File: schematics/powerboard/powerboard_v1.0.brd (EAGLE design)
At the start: 50 x 50 mm, 38 parts, among them IC1 ACS756LCB-100B-PFF-T, IC2 ATMEGA644-A, Y1 10MHZ

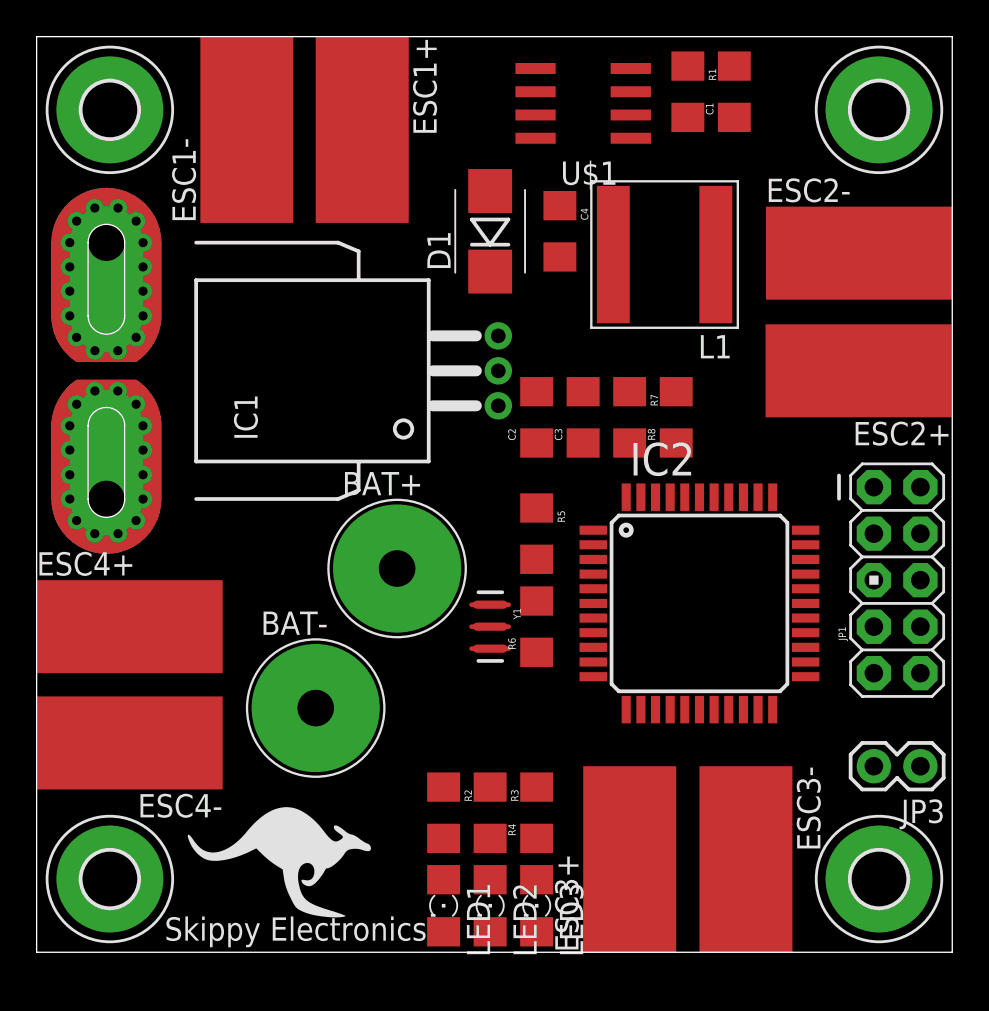
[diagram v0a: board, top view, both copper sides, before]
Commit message: New PCB for power board
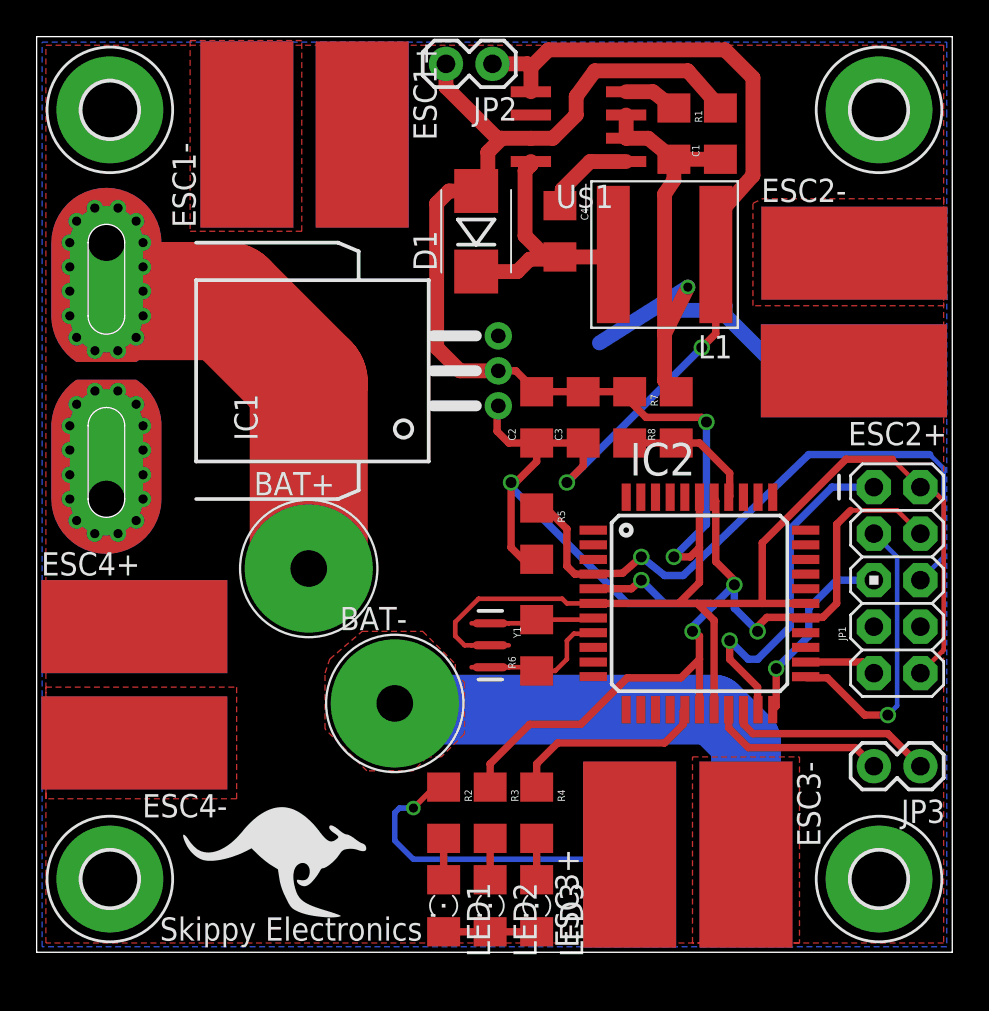
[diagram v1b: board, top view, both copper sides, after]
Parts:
- added JP2: M02PTH, SparkFun-Connectors:1X02
- moved BAT+ 4.83 mm to (14.9, 21.0)
- moved BAT- 4.33 mm to (19.6, 13.6)
- moved C1 2.41 mm to (37.3, 44.7)
- moved R1 2.41 mm to (34.8, 44.7)
- moved U$1 1.30 mm to (29.6, 45.1)
- moved R6 1.02 mm to (27.3, 16.8)
- moved Y1 1.02 mm to (24.8, 16.8)
- moved D1 0.76 mm to (24.0, 39.4)
- moved ESC1+ 0.25 mm to (17.8, 44.7)
- moved ESC1- 0.25 mm to (11.5, 44.7)
- moved ESC2- 0.25 mm to (44.7, 38.2)
- moved PLC1 0.25 mm to (8.00, 1.91)
- moved ESC3+ 0.25 mm to (32.4, 5.33)
- moved ESC3- 0.25 mm to (38.7, 5.33)
- moved ESC4+ 0.25 mm to (5.33, 17.8)
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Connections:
- removed net 5V: IC1.1
- net 3.3V: now also IC1.1, JP2.1
- net GND: now also ESC1-.P$2, ESC2-.P$2, ESC3-.P$2, ESC4-.P$2, JP2.2
- net LO_BATT_LED: now also IC2.16; no longer IC2.30
- net V_BATT: now also ESC1+.P$2, ESC2+.P$2, ESC3+.P$2, ESC4+.P$2
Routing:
- net GND: track 0.00 -> 152.3 mm, vias 0 -> 2
- net 3.3V: track 0.00 -> 124.8 mm, vias 0 -> 7
- net V_BATT: track 0.00 -> 61.5 mm, vias 0 -> 2
- net NSRST: track 0.00 -> 35.2 mm, vias 0 -> 1
- net N$1: track 0.00 -> 22.9 mm
- net TCK: track 0.00 -> 19.7 mm, vias 0 -> 1
- net TDO: track 0.00 -> 16.0 mm, vias 0 -> 1
- net N$2: track 0.00 -> 13.9 mm
- net SDA: track 0.00 -> 11.4 mm
- net LO_BATT_LED: track 0.00 -> 11.0 mm
- net TMS: track 0.00 -> 10.5 mm, vias 0 -> 1
- net SCL: track 0.00 -> 9.79 mm
- net N$10: track 0.00 -> 7.48 mm
- net N$9: track 0.00 -> 6.16 mm
- net N$5: track 0.00 -> 5.06 mm
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- added copper zone on layer 1, net GND
- added copper zone on layer 16, net V_BATT
